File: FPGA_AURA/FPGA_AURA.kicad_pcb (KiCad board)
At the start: 10 copper layers, 50 x 50 mm, 151 parts, among them J1 SS5-40-3.00-X-D-K-XX, J2 SS5-20-3.00-X-D-K-XX, U1 XC7A35T-2FTG256C, U2 W25Q256JVEIQ, U200 ADP5014, U4 TPS51200DRCR, U500 MT41K128M16JT-125_IT_K

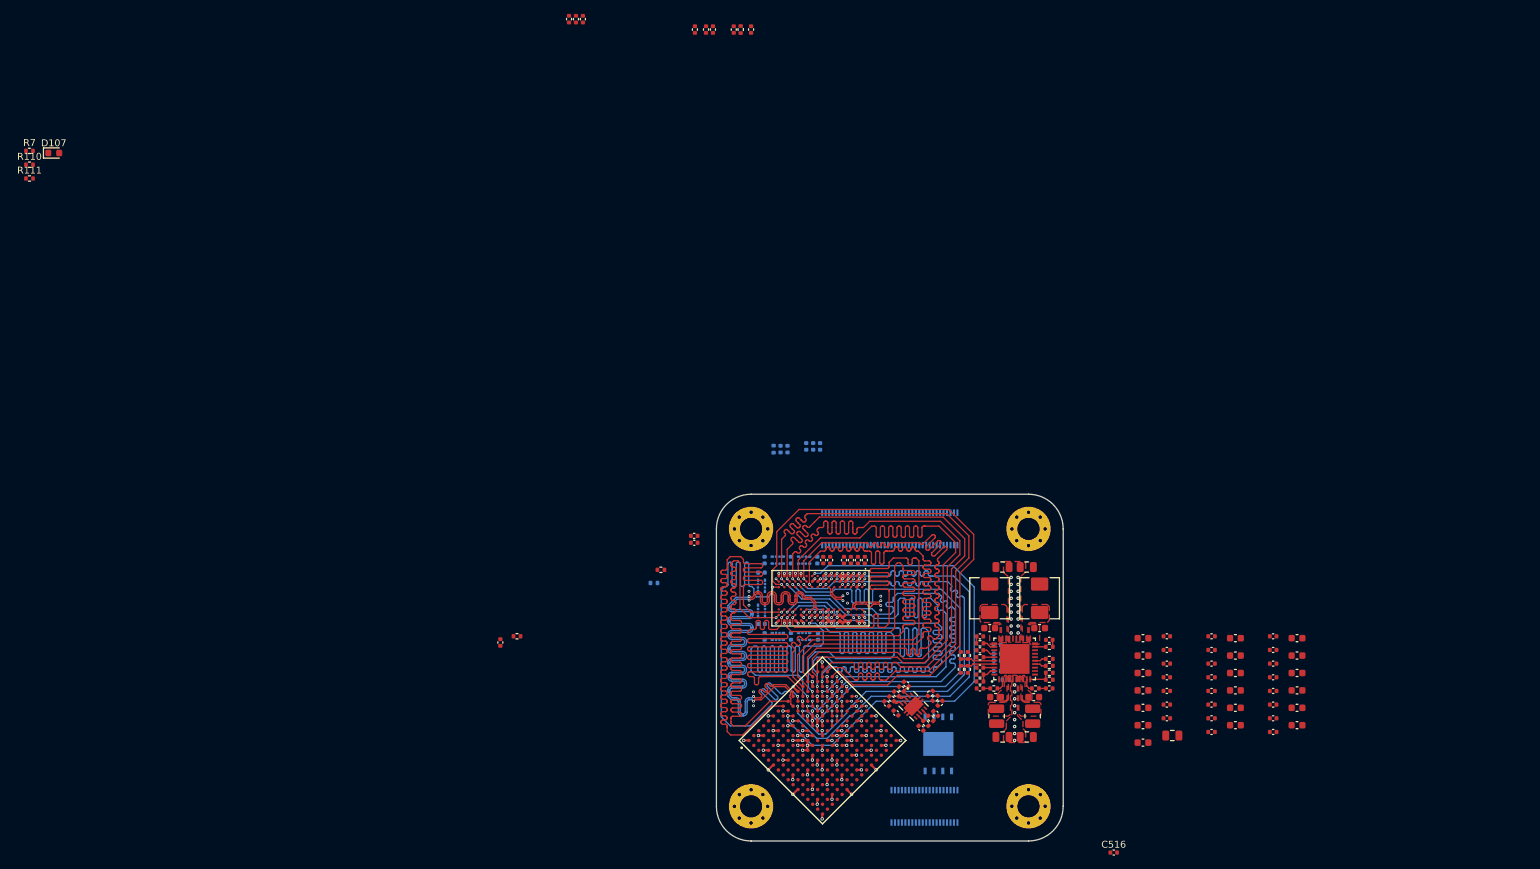
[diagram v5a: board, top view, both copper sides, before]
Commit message: Connector pinnout defined loosly. Next is schematic clean-up followed by routing.
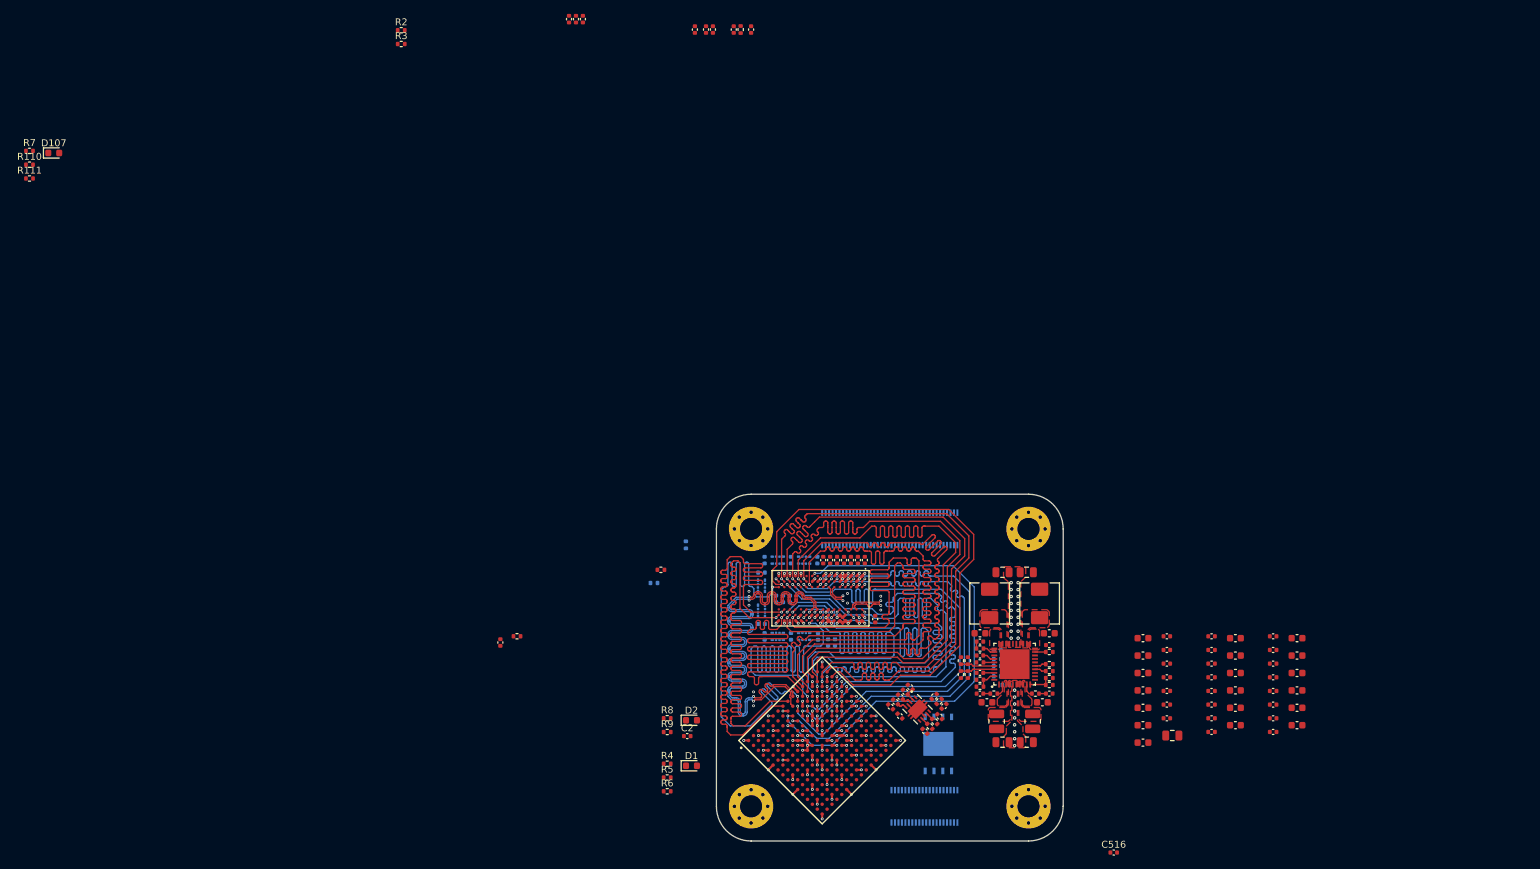
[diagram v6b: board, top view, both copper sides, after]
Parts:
- added C2: 470n, Capacitor_SMD:C_0402_1005Metric, F.Cu at (95.8, 84.9)
- added D1: LED, LED_SMD:LED_0603_1608Metric, F.Cu at (96.4, 89.2)
- added D2: LED, LED_SMD:LED_0603_1608Metric, F.Cu at (96.4, 82.6)
- added R2: 22R, Resistor_SMD:R_0402_1005Metric, F.Cu at (54.6, -16.9)
- added R3: 4k7, Resistor_SMD:R_0402_1005Metric, F.Cu at (54.6, -14.9)
- added R4: 0R, Resistor_SMD:R_0402_1005Metric, F.Cu at (92.9, 88.9)
- added R5: 0R, Resistor_SMD:R_0402_1005Metric, F.Cu at (92.9, 90.8)
- added R6: 330R, Resistor_SMD:R_0402_1005Metric, F.Cu at (92.9, 92.8)
- added R8: 10k, Resistor_SMD:R_0402_1005Metric, F.Cu at (92.9, 82.3)
- added R9: 470R, Resistor_SMD:R_0402_1005Metric, F.Cu at (92.9, 84.3)
- C40, C47: value 47 -> 47u
- R110: value 200R -> 330R
- R7: value 12k -> 100R
- moved C529 28.7 mm to (117.1, 71.4)
- moved C518 28.5 mm to (116.1, 71.4)
- moved C512 28.3 mm to (122.9, 68.0), turned to -90 degrees
- moved C515 22.6 mm to (109.6, 65.1)
- moved C524 22.6 mm to (108.6, 65.1)
- moved C520 21.6 mm to (110.6, 65.1), turned to 90 degrees
- moved C517 20.9 mm to (117.4, 59.5), turned to 90 degrees
- moved R523 18.7 mm to (95.6, 57.3)
- moved C202 1.59 mm to (148.0, 70.0)
- moved C203 1.59 mm to (138.0, 70.0)
- moved C200 1.46 mm to (147.0, 80.0)
- moved C201 1.46 mm to (139.0, 80.0)
- moved C205 0.75 mm to (138.0, 75.8)
- moved C206 0.75 mm to (141.2, 61.2)
- moved C207 0.75 mm to (144.8, 61.2)
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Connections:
- net 100MHz_CC renamed /600_FPGA_Banks_14_15/100MHZ_CLK
- C54 pad 1: +3V3 -> +1V8
- C55 pad 1: +3V3 -> +1V8
- C56 pad 1: +3V3 -> +1V8
- C57 pad 1: +3V3 -> +1V8
- C58 pad 1: +3V3 -> +1V8
- C59 pad 1: +3V3 -> +1V8
- C60 pad 1: +3V3 -> +1V8
- J1 pad 01: unconnected-(J1-Pad01) -> GND
- J1 pad 02: unconnected-(J1-Pad02) -> +5V
- J1 pad 03: unconnected-(J1-Pad03) -> ETH_0_RX_CLK
- J1 pad 04: unconnected-(J1-Pad04) -> GND
- J1 pad 05: unconnected-(J1-Pad05) -> GND
- J1 pad 06: unconnected-(J1-Pad06) -> +5V
- J1 pad 07: unconnected-(J1-Pad07) -> ETH_0_RX_DV
- J1 pad 08: unconnected-(J1-Pad08) -> GND
- J1 pad 09: unconnected-(J1-Pad09) -> ETH_0_CRS
- J1 pad 10: unconnected-(J1-Pad10) -> +5V
- J1 pad 11: unconnected-(J1-Pad11) -> ETH_0_RX_ER
- J1 pad 12: unconnected-(J1-Pad12) -> +5V
- J1 pad 13: unconnected-(J1-Pad13) -> ETH_0_COL
- J1 pad 14: unconnected-(J1-Pad14) -> GND
- J1 pad 15: unconnected-(J1-Pad15) -> GND
- J1 pad 16: unconnected-(J1-Pad16) -> +5V
- J1 pad 17: unconnected-(J1-Pad17) -> ETH_0_RXD_0
- J1 pad 18: unconnected-(J1-Pad18) -> GND
- J1 pad 19: unconnected-(J1-Pad19) -> ETH_0_RXD_1
- J1 pad 20: unconnected-(J1-Pad20) -> +5V
- J1 pad 21: unconnected-(J1-Pad21) -> ETH_0_RXD_2
- J1 pad 22: unconnected-(J1-Pad22) -> +5V
- J1 pad 23: unconnected-(J1-Pad23) -> ETH_0_RXD_3
- J1 pad 24: unconnected-(J1-Pad24) -> GND
- J1 pad 25: unconnected-(J1-Pad25) -> GND
- J1 pad 26: unconnected-(J1-Pad26) -> SPI_1V8_CS_3
- J1 pad 27: unconnected-(J1-Pad27) -> ETH_0_TX_CLK
- J1 pad 28: unconnected-(J1-Pad28) -> GND
- J1 pad 29: unconnected-(J1-Pad29) -> ETH_0_TX_EN
- J1 pad 30: unconnected-(J1-Pad30) -> SPI_1V8_CS_2
- J1 pad 31: unconnected-(J1-Pad31) -> GND
- J1 pad 32: unconnected-(J1-Pad32) -> SPI_1V8_CS_1
- J1 pad 33: unconnected-(J1-Pad33) -> ETH_0_TXD_0
- J1 pad 34: unconnected-(J1-Pad34) -> GND
- J1 pad 35: unconnected-(J1-Pad35) -> ETH_0_TXD_1
- J1 pad 36: unconnected-(J1-Pad36) -> SPI_1V8_CS_0
- J1 pad 37: unconnected-(J1-Pad37) -> ETH_0_TXD_2
- J1 pad 38: unconnected-(J1-Pad38) -> SPI_1V8_SCK
- J1 pad 39: unconnected-(J1-Pad39) -> ETH_0_TXD_3
- J1 pad 40: unconnected-(J1-Pad40) -> GND
- J1 pad 41: unconnected-(J1-Pad41) -> GND
- J1 pad 42: unconnected-(J1-Pad42) -> SPI_1V8_MOSI
- J1 pad 43: unconnected-(J1-Pad43) -> ETH_1_RX_CLK
- J1 pad 44: unconnected-(J1-Pad44) -> GND
- J1 pad 45: unconnected-(J1-Pad45) -> GND
- J1 pad 46: unconnected-(J1-Pad46) -> SPI_1V8_MISO
- J1 pad 47: unconnected-(J1-Pad47) -> ETH_1_RX_DV
- J1 pad 48: unconnected-(J1-Pad48) -> GND
- J1 pad 49: unconnected-(J1-Pad49) -> ETH_1_CRS
- J1 pad 50: unconnected-(J1-Pad50) -> SDA_1V8
- J1 pad 51: unconnected-(J1-Pad51) -> ETH_1_RX_ER
- J1 pad 52: unconnected-(J1-Pad52) -> SCL_1V8
- J1 pad 53: unconnected-(J1-Pad53) -> ETH_1_COL
- J1 pad 54: unconnected-(J1-Pad54) -> GND
- J1 pad 55: unconnected-(J1-Pad55) -> GND
- J1 pad 56: unconnected-(J1-Pad56) -> UART_1V8_0_TX
- J1 pad 57: unconnected-(J1-Pad57) -> ETH_1_RXD_0
- J1 pad 58: unconnected-(J1-Pad58) -> GND
- J1 pad 59: unconnected-(J1-Pad59) -> ETH_1_RXD_1
- J1 pad 60: unconnected-(J1-Pad60) -> UART_1V8_0_RX
- J1 pad 61: unconnected-(J1-Pad61) -> ETH_1_RXD_2
- J1 pad 62: unconnected-(J1-Pad62) -> UART_1V8_1_TX
- J1 pad 63: unconnected-(J1-Pad63) -> ETH_1_RXD_3
- J1 pad 64: unconnected-(J1-Pad64) -> GND
- J1 pad 65: unconnected-(J1-Pad65) -> GND
- J1 pad 66: unconnected-(J1-Pad66) -> UART_1V8_1_RX
- J1 pad 67: unconnected-(J1-Pad67) -> ETH_1_TX_CLK
- J1 pad 68: unconnected-(J1-Pad68) -> GND
- J1 pad 69: unconnected-(J1-Pad69) -> ETH_1_TX_EN
- J1 pad 70: unconnected-(J1-Pad70) -> PHY_0_RST
- J1 pad 71: unconnected-(J1-Pad71) -> GND
- J1 pad 72: unconnected-(J1-Pad72) -> PHY_1_RST
- J1 pad 73: unconnected-(J1-Pad73) -> ETH_1_TXD_0
- J1 pad 74: unconnected-(J1-Pad74) -> GND
- J1 pad 75: unconnected-(J1-Pad75) -> ETH_1_TXD_1
- J1 pad 76: unconnected-(J1-Pad76) -> MDC
- J1 pad 77: unconnected-(J1-Pad77) -> ETH_1_TXD_2
- J1 pad 78: unconnected-(J1-Pad78) -> MDIO
- J1 pad 79: unconnected-(J1-Pad79) -> ETH_1_TXD_3
- J1 pad 80: unconnected-(J1-Pad80) -> GND
- J2 pad 01: unconnected-(J2-Pad01) -> GND
- J2 pad 02: unconnected-(J2-Pad02) -> SYS_nRST
- J2 pad 03: unconnected-(J2-Pad03) -> TMS
- J2 pad 04: unconnected-(J2-Pad04) -> GND
- J2 pad 05: unconnected-(J2-Pad05) -> TCK
- J2 pad 06: unconnected-(J2-Pad06) -> GND
- J2 pad 07: unconnected-(J2-Pad07) -> GND
- J2 pad 08: unconnected-(J2-Pad08) -> FPGA_REFCLK_P
- J2 pad 09: unconnected-(J2-Pad09) -> GND
- J2 pad 10: unconnected-(J2-Pad10) -> FPGA_REFCLK_N
- J2 pad 11: unconnected-(J2-Pad11) -> TDI
- J2 pad 12: unconnected-(J2-Pad12) -> GND
- J2 pad 13: unconnected-(J2-Pad13) -> TDO
- J2 pad 14: unconnected-(J2-Pad14) -> GND
- J2 pad 15: unconnected-(J2-Pad15) -> GND
- J2 pad 16: unconnected-(J2-Pad16) -> SPI_3V3_CS_2
- J2 pad 17: unconnected-(J2-Pad17) -> SPI_3V3_CS_1
- J2 pad 18: unconnected-(J2-Pad18) -> GND
- J2 pad 19: unconnected-(J2-Pad19) -> SPI_3V3_CS_0
- J2 pad 20: unconnected-(J2-Pad20) -> CAN_TX
- J2 pad 21: unconnected-(J2-Pad21) -> GND
- J2 pad 22: unconnected-(J2-Pad22) -> CAN_RX
- J2 pad 23: unconnected-(J2-Pad23) -> SPI_3V3_SCK
- J2 pad 24: unconnected-(J2-Pad24) -> GND
- J2 pad 25: unconnected-(J2-Pad25) -> SPI_3V3_MOSI
- J2 pad 26: unconnected-(J2-Pad26) -> UART_3V3_0_TX
- J2 pad 27: unconnected-(J2-Pad27) -> SPI_3V3_MISO
- J2 pad 28: unconnected-(J2-Pad28) -> UART_3V3_0_RX
- J2 pad 29: unconnected-(J2-Pad29) -> GND
- J2 pad 30: unconnected-(J2-Pad30) -> GND
- J2 pad 31: unconnected-(J2-Pad31) -> SPI_SD_CS_0
- J2 pad 32: unconnected-(J2-Pad32) -> UART_3V3_1_TX
- J2 pad 33: unconnected-(J2-Pad33) -> SPI_SD_SCK
- J2 pad 34: unconnected-(J2-Pad34) -> UART_3V3_1_RX
- J2 pad 35: unconnected-(J2-Pad35) -> SPI_SD_MOSI
- J2 pad 36: unconnected-(J2-Pad36) -> GND
- J2 pad 37: unconnected-(J2-Pad37) -> SPI_SD_MISO
- J2 pad 38: unconnected-(J2-Pad38) -> SDA_3V3
- J2 pad 39: unconnected-(J2-Pad39) -> GND
- J2 pad 40: unconnected-(J2-Pad40) -> SCL_3V3
- R7 pad 1: +3V3 -> /400_FPGA_Config/INIT_LED
- U1 pad A2: unconnected-(U1F-IO_L8N_T1_AD14N_35-PadA2) -> ETH_1_TX_EN
- U1 pad B1: unconnected-(U1F-IO_L9N_T1_DQS_AD7N_35-PadB1) -> ETH_1_TXD_1
- U1 pad C1: unconnected-(U1F-IO_L9P_T1_DQS_AD7P_35-PadC1) -> ETH_1_TXD_0
- U1 pad D1: unconnected-(U1F-IO_L10N_T1_AD15N_35-PadD1) -> ETH_1_TXD_3
- U1 pad D4: unconnected-(U1F-IO_L12P_T1_MRCC_35-PadD4) -> ETH_1_RX_CLK
- U1 pad E1: ETH_1_RX_2 -> ETH_1_RXD_0
- U1 pad E2: unconnected-(U1F-IO_L10P_T1_AD15P_35-PadE2) -> ETH_1_TXD_2
- U1 pad E3: unconnected-(U1F-IO_L11P_T1_SRCC_35-PadE3) -> ETH_1_TX_CLK
- U1 pad E5: ETH_1_RXC -> unconnected-(U1F-IO_L13N_T2_MRCC_35-PadE5)
- U1 pad F2: ETH_1_RX_1 -> ETH_1_COL
- U1 pad F3: ETH_1_RX_0 -> ETH_1_CRS
- U1 pad F4: unconnected-(U1F-IO_L14P_T2_SRCC_35-PadF4) -> ETH_0_TX_CLK
- U1 pad F5: ETH_0_RXC -> ETH_0_RX_CLK
- U1 pad G1: ETH_1_TD_1 -> ETH_1_RX_ER
- U1 pad G2: ETH_1_TD_0 -> ETH_1_RXD_3
- U1 pad G4: ETH_1_RX_CTL -> ETH_1_RXD_2
- U1 pad G5: ETH_1_RX_3 -> ETH_1_RXD_1
- U1 pad H1: ETH_0_RX_1 -> ETH_0_RXD_1
- U1 pad H2: ETH_0_RX_0 -> ETH_0_RXD_0
- U1 pad H3: ETH_0_RX_3 -> ETH_0_RXD_3
- U1 pad H4: ETH_1_TD_3 -> unconnected-(U1F-IO_L18N_T2_35-PadH4)
- U1 pad H5: ETH_1_TD_2 -> ETH_1_RX_DV
- U1 pad J1: ETH_0_TD_0 -> ETH_0_RX_DV
- U1 pad J3: ETH_0_RX_2 -> ETH_0_RXD_2
- U1 pad J4: ETH_1_TXC -> ETH_0_COL
- U1 pad J5: ETH_1_TX_CTL -> ETH_0_CRS
- U1 pad K1: ETH_0_RX_CTL -> ETH_0_RX_ER
- U1 pad K2: ETH_0_TX_CTL -> ETH_0_TXD_3
- U1 pad K3: ETH_0_TD_3 -> ETH_0_TXD_2
- U1 pad K5: ETH_0_TXC -> ETH_0_TX_EN
- U1 pad L2: ETH_0_TD_2 -> ETH_0_TXD_1
- U1 pad L3: ETH_0_TD_1 -> ETH_0_TXD_0
- U1 pad L7: unconnected-(U1A-TCK_0-PadL7) -> TCK
- U1 pad L9: unconnected-(U1A-PROGRAM_B_0-PadL9) -> /400_FPGA_Config/PROG_B
- U1 pad M1: unconnected-(U1E-IO_L2N_T0_34-PadM1) -> SPI_1V8_CS_1
- U1 pad M11: GND -> /400_FPGA_Config/M2_0
- U1 pad M14: INIT_CALIB_DONE -> /600_FPGA_Banks_14_15/INIT_CALIB
- U1 pad M2: unconnected-(U1E-IO_L2P_T0_34-PadM2) -> SPI_1V8_CS_2
- U1 pad M3: +3V3 -> +1V8
- U1 pad M4: unconnected-(U1E-IO_L1N_T0_34-PadM4) -> SPI_1V8_CS_3
- U1 pad M5: unconnected-(U1E-IO_L6P_T0_34-PadM5) -> SDA_1V8
- U1 pad M6: SPI_CS -> SPI_3V3_SCK
- U1 pad M7: unconnected-(U1A-TMS_0-PadM7) -> TMS
- U1 pad N1: unconnected-(U1E-IO_L4P_T0_34-PadN1) -> SPI_1V8_SCK
- U1 pad N14: unconnected-(U1C-IO_L12P_T1_MRCC_14-PadN14) -> FPGA_REFCLK_P
- U1 pad N16: unconnected-(U1C-IO_L7N_T1_D10_14-PadN16) -> SPI_SD_CS_0
- U1 pad N3: unconnected-(U1E-IO_L3P_T0_DQS_34-PadN3) -> SPI_1V8_CS_0
- U1 pad N4: unconnected-(U1E-IO_L6N_T0_VREF_34-PadN4) -> SCL_1V8
- U1 pad N6: SPI_SCK -> SPI_3V3_MOSI
- U1 pad N7: unconnected-(U1A-TDI_0-PadN7) -> TDI
- U1 pad N8: unconnected-(U1A-TDO_0-PadN8) -> TDO
- U1 pad N9: unconnected-(U1C-IO_L18P_T2_A12_D28_14-PadN9) -> SPI_3V3_CS_0
- U1 pad P1: unconnected-(U1E-IO_L4N_T0_34-PadP1) -> SPI_1V8_MOSI
- U1 pad P10: unconnected-(U1C-IO_L14P_T2_SRCC_14-PadP10) -> CAN_TX
- U1 pad P11: unconnected-(U1C-IO_L14N_T2_SRCC_14-PadP11) -> CAN_RX
- U1 pad P14: unconnected-(U1C-IO_L12N_T1_MRCC_14-PadP14) -> FPGA_REFCLK_N
- U1 pad P15: unconnected-(U1C-IO_L8P_T1_D11_14-PadP15) -> SPI_SD_SCK
- U1 pad P16: unconnected-(U1C-IO_L8N_T1_D12_14-PadP16) -> SPI_SD_MOSI
- U1 pad P4: unconnected-(U1E-IO_L5P_T0_34-PadP4) -> SPI_1V8_MISO
- U1 pad P8: SPI_MOSI -> SPI_3V3_MISO
- U1 pad R1: unconnected-(U1E-IO_L7N_T1_34-PadR1) -> UART_1V8_0_TX
- U1 pad R10: unconnected-(U1C-IO_L17P_T2_A14_D30_14-PadR10) -> SPI_3V3_CS_2
- U1 pad R11: unconnected-(U1C-IO_L17N_T2_A13_D29_14-PadR11) -> SPI_3V3_CS_1
- U1 pad R15: unconnected-(U1C-IO_L9P_T1_DQS_14-PadR15) -> SPI_SD_MISO
- U1 pad R3: unconnected-(U1E-IO_L8P_T1_34-PadR3) -> UART_1V8_0_RX
- U1 pad R4: +3V3 -> +1V8
- U1 pad R5: unconnected-(U1C-IO_L23P_T3_A03_D19_14-PadR5) -> UART_3V3_0_RX
- U1 pad R6: UART_TX -> UART_3V3_1_TX
- U1 pad R7: UART_RX -> UART_3V3_1_RX
- U1 pad R8: SPI_MISO -> unconnected-(U1C-IO_L20N_T3_A07_D23_14-PadR8)
- U1 pad T1: +3V3 -> +1V8
- U1 pad T10: unconnected-(U1C-IO_L22N_T3_A04_D20_14-PadT10) -> UART_3V3_0_TX
- U1 pad T3: unconnected-(U1E-IO_L9N_T1_DQS_34-PadT3) -> UART_1V8_1_RX
- U1 pad T4: unconnected-(U1E-IO_L9P_T1_DQS_34-PadT4) -> UART_1V8_1_TX
- U1 pad T7: unconnected-(U1C-IO_L21P_T3_DQS_14-PadT7) -> SDA_3V3
- U1 pad T8: unconnected-(U1C-IO_L21N_T3_DQS_A06_D22_14-PadT8) -> SCL_3V3
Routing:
- net +3V3: track 11.9 -> 9.78 mm, vias 16 -> 13
- net +1V8: track 4.24 -> 6.36 mm, vias 5 -> 8
- net /200_Power_Regulation/ADP_RC2: track 1.01 -> 0.00 mm
- net /500_DDR3L/DDR3_ZQ: track 0.00 -> 0.57 mm, vias 0 -> 1
